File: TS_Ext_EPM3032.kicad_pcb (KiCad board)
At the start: 2 copper layers, 94 x 74.3 mm, 52 parts, among them J1 JTAG, J2 CD_IN, J3 System Ext, J4 AUDIO OUT, J5 SJ1-3525N, Q1 BC547, U1 EPM3032ALC44, U2 AMS1117, U3 YM2149, U4 YM2149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

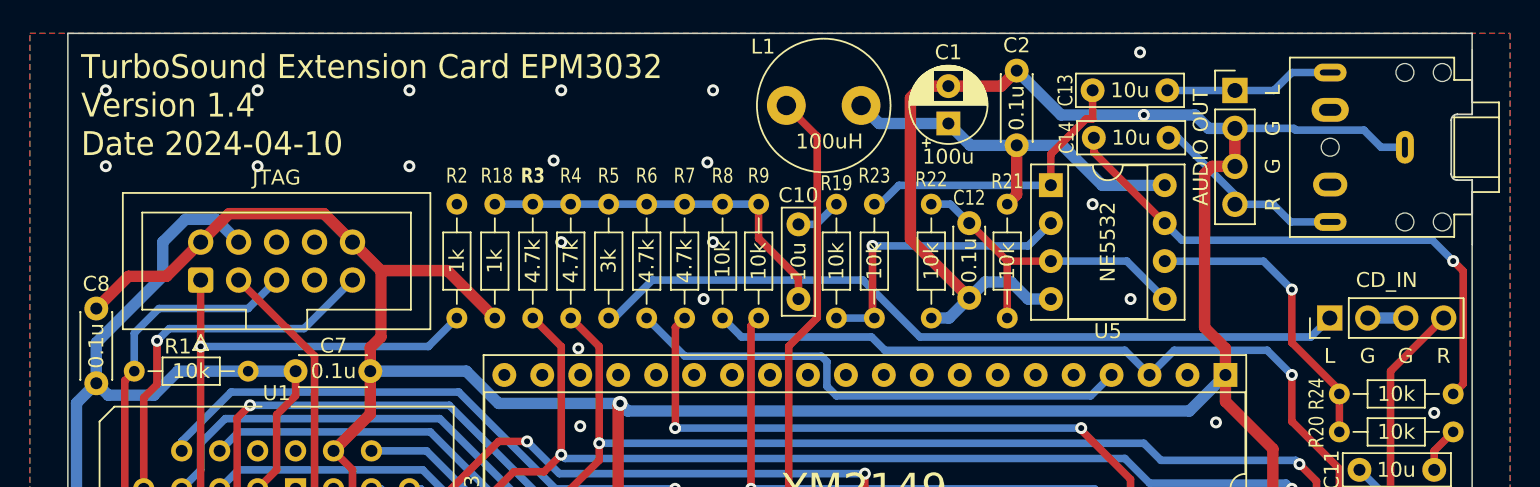
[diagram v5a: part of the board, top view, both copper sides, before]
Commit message: Change C13/C14 to electrolytic
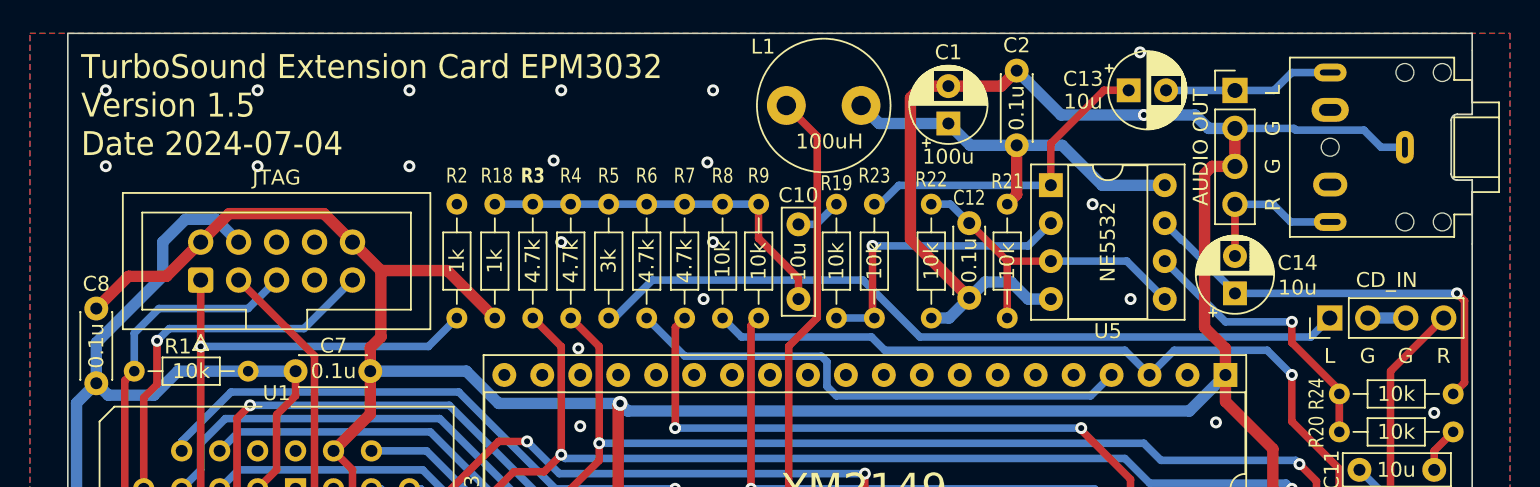
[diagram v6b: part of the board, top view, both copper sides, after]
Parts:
- C13, C14: footprint Capacitor_THT:C_Rect_L7.0mm_W2.0mm_P5.00mm -> Capacitor_THT:CP_Radial_D5.0mm_P2.50mm
- moved C14 11.3 mm to (106.0, 42.8), turned to 90 degrees
- moved C13 2.41 mm to (98.9, 29.2)
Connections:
- C14 pad 1: /ROUT -> Net-(C14-Pad1)
- C14 pad 2: Net-(C14-Pad2) -> /ROUT
- R24 pad 2: Net-(C14-Pad2) -> Net-(C14-Pad1)
- U5 pad 7: Net-(C14-Pad2) -> Net-(C14-Pad1)
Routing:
- net Net-(C14-Pad2): track 37.5 -> 0.00 mm, vias 1 -> 0
- net Net-(C14-Pad1): track 0.00 -> 28.8 mm, vias 0 -> 1
- net /ROUT: track 13.5 -> 10.3 mm
- net Net-(C13-Pad1): track 19.7 -> 21.4 mm
- net Net-(U5B--): track 19.9 -> 18.6 mm
